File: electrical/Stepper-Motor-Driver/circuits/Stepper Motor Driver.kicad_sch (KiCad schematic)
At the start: 18 parts, among them J3 Screw_Terminal_01x04

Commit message: Initial PCB layout
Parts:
- added H1, H2, H3, H4: MountingHole_Pad, MountingHole:MountingHole_2.2mm_M2_DIN965_Pad, symbol Mechanical:MountingHole_Pad
- added J1: Screw_Terminal_01x03, TerminalBlock_MetzConnect:TerminalBlock_MetzConnect_Type011_RT05503HBLC_1x03_P5.00mm_Horizontal, symbol Connector:Screw_Terminal_01x03
- J2: renamed from J3; footprint (none) -> TerminalBlock_MetzConnect:TerminalBlock_MetzConnect_Type011_RT05504HBLC_1x04_P5.00mm_Horizontal
- renumbered C15 to C1, C16 to C2, C17 to C3, C18 to C4, C19 to C5, C20 to C6, C21 to C7, C22 to C8, U13 to U1
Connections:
- net Current Sensor B/IN-: now also J2.4 (Pin_4); no longer J2.3 (Pin_3)
- net GND: now also H1.1, H2.1, H3.1, H4.1
- net H-Bridge Controller B/BR2: now also J2.3 (Pin_3); no longer J2.4 (Pin_4)
- net Power/GND: now also J1.2 (Pin_2)
- new net Power/+12VIn: J1.1 (Pin_1)
- new net Power/+VMotor: J1.3 (Pin_3)
- no-connect marks 9 -> 27
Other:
- sheet Power ports: added +12VIn, +VMotor; removed 24V
- note added: "Connect terminal 1 to coil A and back to terminal 2. Connect terminal 4 to coil B and back to terminal 3."
- note removed: "Connect terminal 1 to coil A and back to terminal 2. Connect terminal 3 to coil B and back to terminal 4."

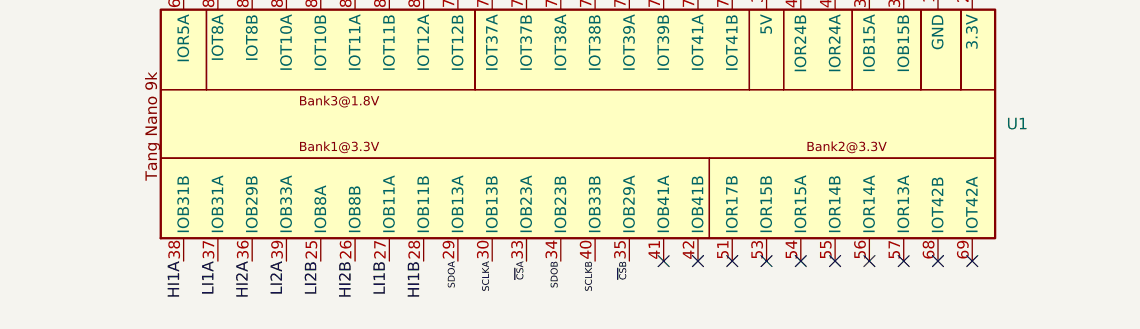
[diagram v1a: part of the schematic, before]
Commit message: Redoing FPGA pin assignment to optimize signal trace lengths
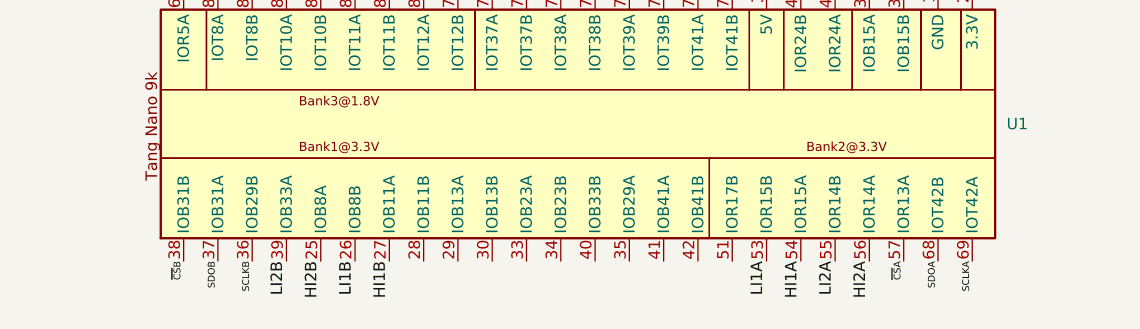
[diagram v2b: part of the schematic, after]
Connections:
- net HI1A: now also U1.54 (IOR15A); no longer U1.38 (IOB31B)
- net HI1B: now also U1.27 (IOB11A); no longer U1.28 (IOB11B)
- net HI2A: now also U1.56 (IOR14A); no longer U1.36 (IOB29B)
- net HI2B: now also U1.25 (IOB8A); no longer U1.26 (IOB8B)
- net LI1A: now also U1.53 (IOR15B); no longer U1.37 (IOB31A)
- net LI1B: now also U1.26 (IOB8B); no longer U1.27 (IOB11A)
- net LI2A: now also U1.55 (IOR14B); no longer U1.39 (IOB33A)
- net LI2B: now also U1.39 (IOB33A); no longer U1.25 (IOB8A)
- net SCLKA: now also U1.69 (IOT42A); no longer U1.30 (IOB13B)
- net SCLKB: now also U1.36 (IOB29B); no longer U1.40 (IOB33B)
- net SDOA: now also U1.68 (IOT42B); no longer U1.29 (IOB13A)
- net SDOB: now also U1.37 (IOB31A); no longer U1.34 (IOB23B)
- net ~{CS}A: now also U1.57 (IOR13A); no longer U1.33 (IOB23A)
- net ~{CS}B: now also U1.38 (IOB31B); no longer U1.35 (IOB29A)
- no-connect marks 27 -> 17
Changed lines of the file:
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@@
-	)
-	(no_connect
-		(at 109.22 167.64)
-	)
-	(no_connect
-		(at 93.98 167.64)
 	)
 	(no_connect
@@
 	)
 	(no_connect
-		(at 97.79 167.64)
-	)
-	(no_connect
-		(at 113.03 167.64)
-	)
-	(no_connect
 		(at 63.5 137.16)
 	)
 	(no_connect
-		(at 105.41 167.64)
-	)
-	(no_connect
 		(at 59.69 137.16)
 	)
@@
 	)
 	(no_connect
-		(at 101.6 167.64)
-	)
-	(no_connect
 		(at 71.12 137.16)
 	)
 	(no_connect
-		(at 120.65 167.64)
-	)
-	(no_connect
 		(at 40.64 137.16)
 	)
@@
 	)
 	(no_connect
-		(at 90.17 167.64)
-	)
-	(no_connect
 		(at 101.6 137.16)
 	)
 	(no_connect
-		(at 124.46 167.64)
-	)
-	(no_connect
 		(at 48.26 137.16)
 	)
@@
 	(no_connect
 		(at 105.41 137.16)
-	)
-	(no_connect
-		(at 116.84 167.64)
 	)
 	(no_connect
@@
 		)
 	)
-	(label "SCLKA"
-		(at 71.12 167.64 270)
-		(effects
-			(font
-				(size 0.762 0.762)
-			)
-			(justify right bottom)
-		)
-	)
-	(label "HI1A"
-		(at 36.83 167.64 270)
+	(label "LI2A"
+		(at 109.22 167.64 270)
 		(effects
 			(font
@@
 	)
 	(label "LI2B"
-		(at 52.07 167.64 270)
+		(at 48.26 167.64 270)
 		(effects
 			(font
@@
 		)
 	)
+	(label "~{CS}B"
+		(at 36.83 167.64 270)
+		(effects
+			(font
+				(size 0.762 0.762)
+			)
+			(justify right bottom)
+		)
+	)
 	(label "LI1A"
 		(at 52.07 64.77 270)
@@
 		)
 	)
+	(label "SDOA"
+		(at 120.65 167.64 270)
+		(effects
+			(font
+				(size 0.762 0.762)
+			)
+			(justify right bottom)
+		)
+	)
 	(label "SCLKA"
 		(at 138.43 57.15 0)
@@
 		)
 	)
-	(label "~{CS}A"
-		(at 74.93 167.64 270)
+	(label "HI1A"
+		(at 105.41 167.64 270)
+		(effects
+			(font
+				(size 1.27 1.27)
+			)
+			(justify right bottom)
+		)
+	)
+	(label "SCLKA"
+		(at 124.46 167.64 270)
 		(effects
 			(font
@@
 		)
 	)
-	(label "HI2B"
-		(at 55.88 167.64 270)
-		(effects
-			(font
-				(size 1.27 1.27)
-			)
-			(justify right bottom)
-		)
-	)
-	(label "~{CS}B"
-		(at 86.36 167.64 270)
+	(label "~{CS}A"
+		(at 116.84 167.64 270)
 		(effects
 			(font
 				(size 0.762 0.762)
+			)
+			(justify right bottom)
+		)
+	)
+	(label "HI1B"
+		(at 59.69 167.64 270)
+		(effects
+			(font
+				(size 1.27 1.27)
 			)
 			(justify right bottom)
@@
 		)
 	)
-	(label "SDOB"
-		(at 78.74 167.64 270)
-		(effects
-			(font
-				(size 0.762 0.762)
-			)
-			(justify right bottom)
-		)
-	)
 	(label "MICROSTEP_BIT2"
 		(at 86.36 137.16 90)
@@
 		)
 	)
-	(label "LI1B"
-		(at 59.69 167.64 270)
-		(effects
-			(font
-				(size 1.27 1.27)
-			)
-			(justify right bottom)
-		)
-	)
-	(label "LI1A"
-		(at 40.64 167.64 270)
-		(effects
-			(font
-				(size 1.27 1.27)
-			)
-			(justify right bottom)
-		)
-	)
 	(label "HI1B"
 		(at 260.35 64.77 270)
@@
 		)
 	)
-	(label "SDOA"
-		(at 67.31 167.64 270)
+	(label "LI1A"
+		(at 101.6 167.64 270)
+		(effects
+			(font
+				(size 1.27 1.27)
+			)
+			(justify right bottom)
+		)
+	)
+	(label "HI2B"
+		(at 52.07 167.64 270)
+		(effects
+			(font
+				(size 1.27 1.27)
+			)
+			(justify right bottom)
+		)
+	)
+	(label "HI2A"
+		(at 113.03 167.64 270)
+		(effects
+			(font
+				(size 1.27 1.27)
+			)
+			(justify right bottom)
+		)
+	)
+	(label "LI1B"
+		(at 55.88 167.64 270)
+		(effects
+			(font
+				(size 1.27 1.27)
+			)
+			(justify right bottom)
+		)
+	)
+	(label "SDOB"
+		(at 40.64 167.64 270)
 		(effects
 			(font
@@
 		)
 	)
-	(label "LI2A"
-		(at 48.26 167.64 270)
-		(effects
-			(font
-				(size 1.27 1.27)
-			)
-			(justify right bottom)
-		)
-	)
-	(label "HI2A"
+	(label "SCLKB"
 		(at 44.45 167.64 270)
 		(effects
 			(font
-				(size 1.27 1.27)
-			)
-			(justify right bottom)
-		)
-	)
-	(label "SCLKB"
-		(at 82.55 167.64 270)
-		(effects
-			(font
 				(size 0.762 0.762)
 			)
 			(justify right bottom)
-		)
-	)
-	(label "HI1B"
-		(at 63.5 167.64 270)
-		(effects
-			(font
-				(size 1.27 1.27)
-			)
-			(justify right bottom)

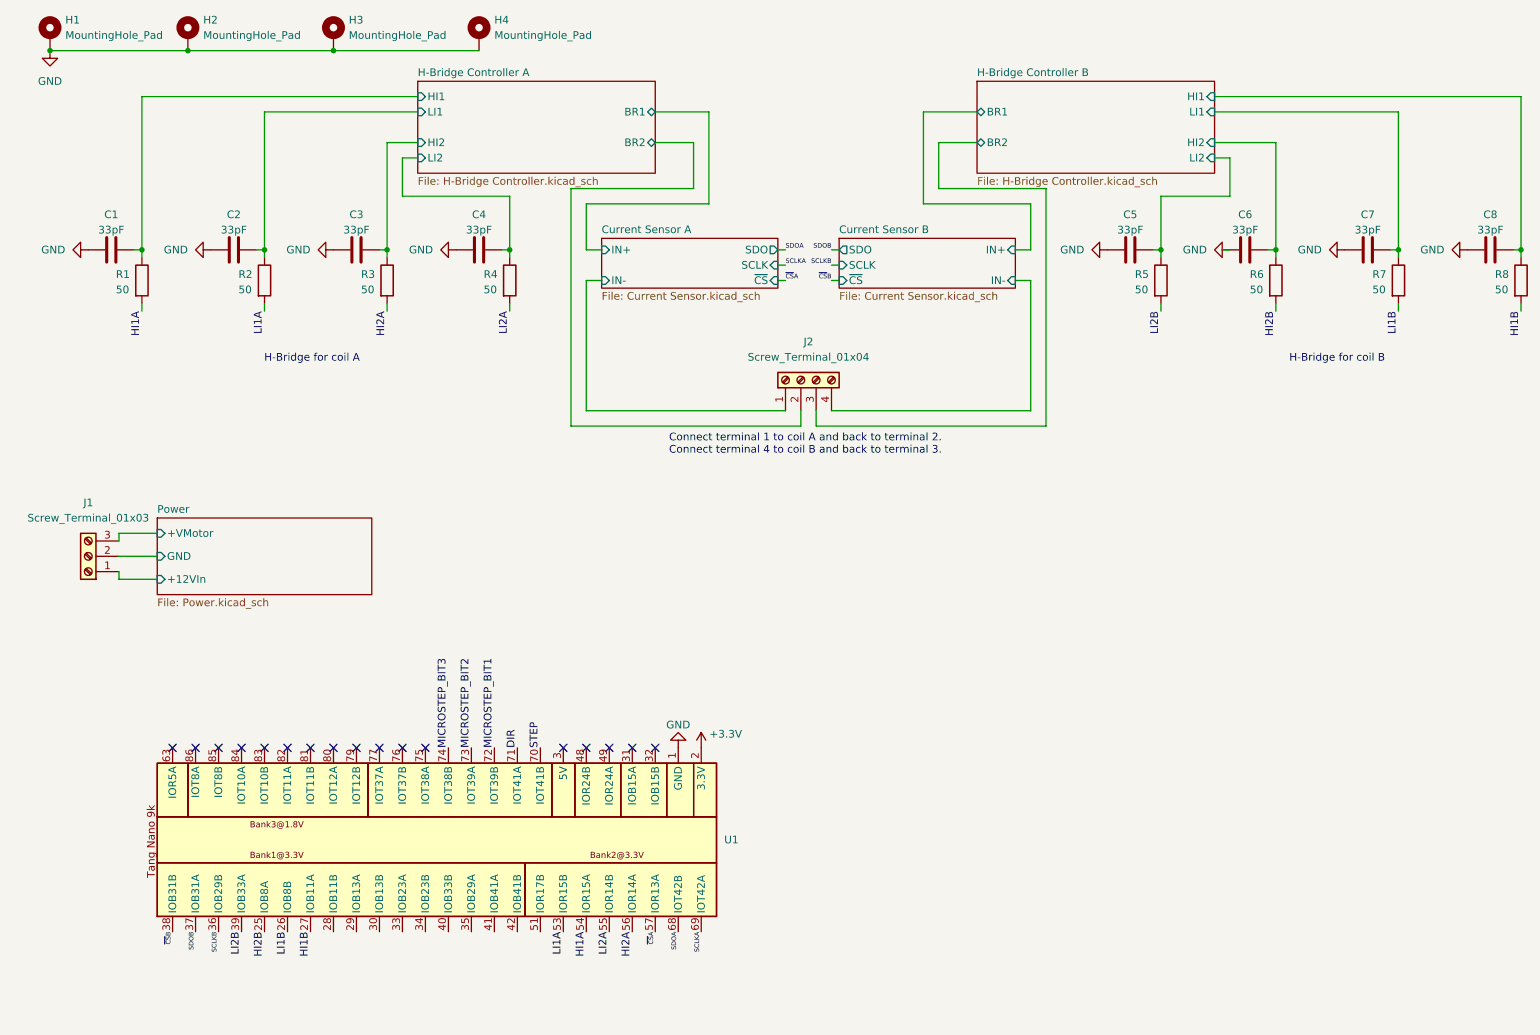
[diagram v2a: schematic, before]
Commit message: Adding series termination resistors for high frequency digital signals
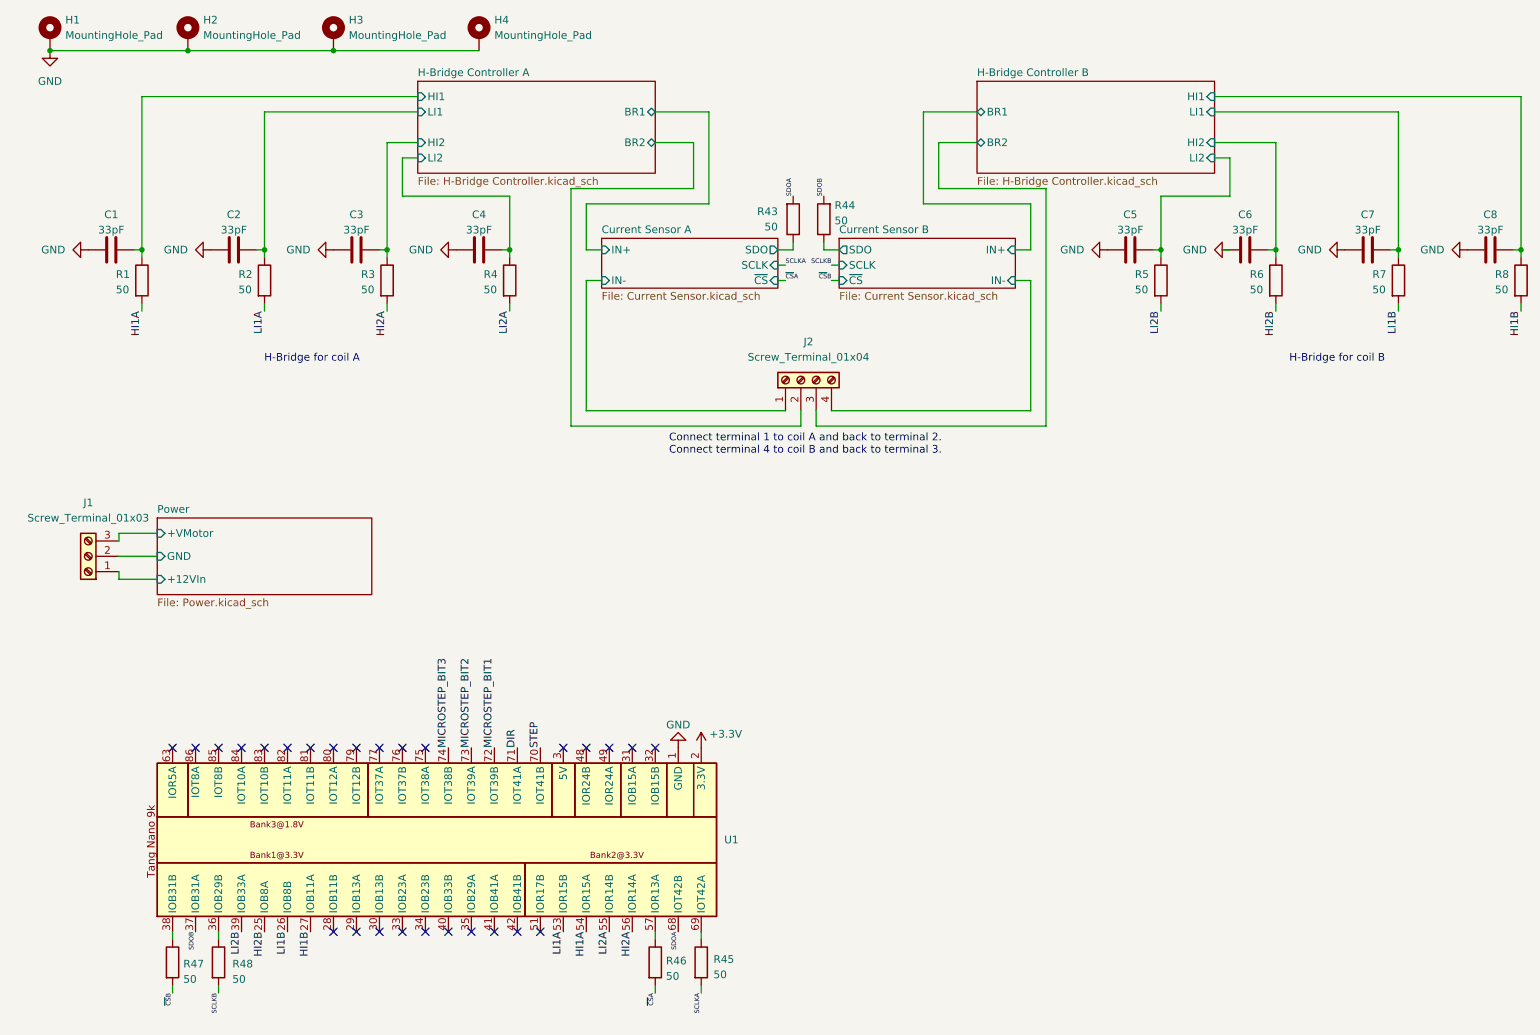
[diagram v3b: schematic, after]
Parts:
- added R43, R44, R45, R46, R47, R48: 50, Resistor_SMD:R_1206_3216Metric, symbol Device:R
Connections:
- net SCLKA: now also R45.2; no longer U1.69 (IOT42A)
- net SCLKB: now also R48.2; no longer U1.36 (IOB29B)
- net SDOA: now also R43.2
- net SDOB: now also R44.2
- net ~{CS}A: now also R46.2; no longer U1.57 (IOR13A)
- net ~{CS}B: now also R47.2; no longer U1.38 (IOB31B)
- new net: R45.1, U1.69 (IOT42A)
- new net: R46.1, U1.57 (IOR13A)
- new net: R48.1, U1.36 (IOB29B)
- new net: R47.1, U1.38 (IOB31B)
- new net Current Sensor A/SDO: R43.1
- new net Current Sensor B/SDO: R44.1
- no-connect marks 17 -> 27

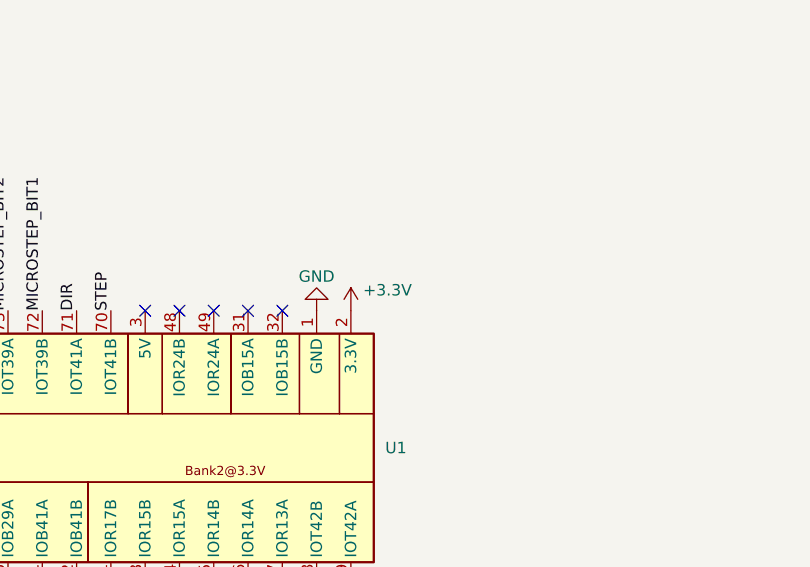
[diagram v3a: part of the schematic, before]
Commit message: Adding missing decoupling for FPGA 3.3V
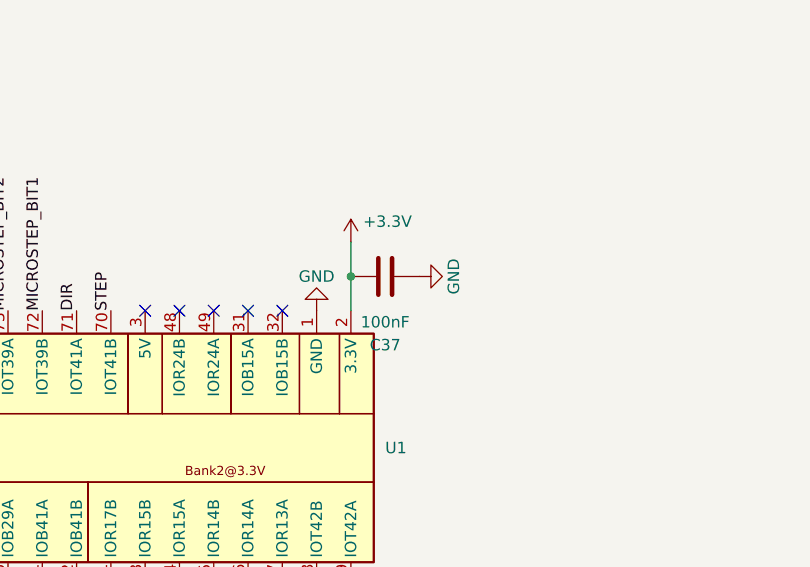
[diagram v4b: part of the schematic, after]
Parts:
- added C37: 100nF, Capacitor_SMD:C_1206_3216Metric, symbol Device:C
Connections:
- net +3.3V: now also C37.1
- net GND: now also C37.2
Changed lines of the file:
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@@
 	)
 	(junction
+		(at 124.46 133.35)
+		(diameter 0)
+		(color 0 0 0 0)
+	)
+	(junction
 		(at 260.35 54.61)
 		(diameter 0)
@@
 	(wire
 		(pts
+			(xy 124.46 133.35) (xy 124.46 137.16)
+		)
+		(stroke
+			(width 0)
+			(type default)
+		)
+	)
+	(wire
+		(pts
 			(xy 125.73 46.99) (xy 105.41 46.99)
 		)
@@
 	(wire
 		(pts
+			(xy 124.46 129.54) (xy 124.46 133.35)
+		)
+		(stroke
+			(width 0)
+			(type default)
+		)
+	)
+	(wire
+		(pts
 			(xy 200.66 63.5) (xy 200.66 64.77)
 		)
@@
 	(symbol
 		(lib_id "power:+3.3V")
-		(at 124.46 137.16 0)
+		(at 124.46 129.54 0)
 		(unit 1)
 		(body_style 1)
@@
 		(dnp no)
 		(property "Reference" "#PWR07"
-			(at 124.46 140.97 0)
+			(at 124.46 133.35 0)
 			(hide yes)
 			(show_name no)
@@
 		)
 		(property "Value" "+3.3V"
-			(at 128.524 134.874 0)
+			(at 128.524 127.254 0)
 			(show_name no)
 			(do_not_autoplace no)
@@
 		)
 		(property "Footprint" ""
-			(at 124.46 137.16 0)
+			(at 124.46 129.54 0)
 			(hide yes)
 			(show_name no)
@@
 		)
 		(property "Datasheet" ""
-			(at 124.46 137.16 0)
+			(at 124.46 129.54 0)
 			(hide yes)
 			(show_name no)
@@
 		)
 		(property "Description" "Power symbol creates a global label with name \"+3.3V\""
-			(at 124.46 137.16 0)
+			(at 124.46 129.54 0)
 			(hide yes)
 			(show_name no)
@@
 	)
 	(symbol
+		(lib_id "power:GND")
+		(at 132.08 133.35 90)
+		(unit 1)
+		(body_style 1)
+		(exclude_from_sim no)
+		(in_bom yes)
+		(on_board yes)
+		(in_pos_files yes)
+		(dnp no)
+		(property "Reference" "#PWR017"
+			(at 138.43 133.35 0)
+			(hide yes)
+			(show_name no)
+			(do_not_autoplace no)
+			(effects
+				(font
+					(size 1.27 1.27)
+				)
+			)
+		)
+		(property "Value" "GND"
+			(at 135.89 133.35 0)
+			(show_name no)
+			(do_not_autoplace no)
+			(effects
+				(font
+					(size 1.27 1.27)
+				)
+			)
+		)
+		(property "Footprint" ""
+			(at 132.08 133.35 0)
+			(hide yes)
+			(show_name no)
+			(do_not_autoplace no)
+			(effects
+				(font
+					(size 1.27 1.27)
+				)
+			)
+		)
+		(property "Datasheet" ""
+			(at 132.08 133.35 0)
+			(hide yes)
+			(show_name no)
+			(do_not_autoplace no)
+			(effects
+				(font
+					(size 1.27 1.27)
+				)
+			)
+		)
+		(property "Description" "Power symbol creates a global label with name \"GND\" , ground"
+			(at 132.08 133.35 0)
+			(hide yes)
+			(show_name no)
+			(do_not_autoplace no)
+			(effects
+				(font
+					(size 1.27 1.27)
+				)
+			)
+		)
+		(pin "1"
+		)
+		(instances
+			(project "Stepper Motor Driver"
+				(path "/c25060f1-f2f3-4cbd-b6ee-5f66e19502f5"
+					(reference "#PWR017")
+					(unit 1)
+				)
+			)
+		)
+	)
+	(symbol
 		(lib_id "Device:C")
 		(at 195.58 54.61 90)
@@
 					(unit 1)
 				)
+			)
+		)
+	)
+	(symbol
+		(lib_id "Device:C")
+		(at 128.27 133.35 90)
+		(unit 1)
+		(body_style 1)
+		(exclude_from_sim no)
+		(in_bom yes)
+		(on_board yes)
+		(in_pos_files yes)
+		(dnp no)
+		(property "Reference" "C37"
+			(at 128.27 140.97 90)
+			(show_name no)
+			(do_not_autoplace no)
+			(effects
+				(font
+					(size 1.27 1.27)
+				)
+			)
+		)
+		(property "Value" "100nF"
+			(at 128.27 138.43 90)
+			(show_name no)
+			(do_not_autoplace no)
+			(effects
+				(font
+					(size 1.27 1.27)
+				)
+			)
+		)
+		(property "Footprint" "Capacitor_SMD:C_1206_3216Metric"
+			(at 132.08 132.3848 0)
+			(hide yes)
+			(show_name no)
+			(do_not_autoplace no)
+			(effects
+				(font
+					(size 1.27 1.27)
+				)
+			)
+		)
+		(property "Datasheet" ""
+			(at 128.27 133.35 0)
+			(hide yes)
+			(show_name no)
+			(do_not_autoplace no)
+			(effects
+				(font
+					(size 1.27 1.27)
+				)
+			)
+		)
+		(property "Description" "Unpolarized capacitor"
+			(at 128.27 133.35 0)
+			(hide yes)
+			(show_name no)
+			(do_not_autoplace no)
+			(effects
+				(font
+					(size 1.27 1.27)
+				)
+			)
+		)
+		(pin "1"
+		)
+		(pin "2"
+		)
+		(instances
+			(project "Stepper Motor Driver"
+				(path "/c25060f1-f2f3-4cbd-b6ee-5f66e19502f5"
+					(reference "C37")
+					(unit 1)
+				)
